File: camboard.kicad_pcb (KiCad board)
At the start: 2 copper layers, 64 x 120.5 mm, 68 parts, among them J1 Conn_02x05_Odd_Even, J2 Conn_02x25_Counter_Clockwise, J3 Conn_02x12_Counter_Clockwise, J4 USB_B_Micro, J5 Conn_01x03, SW1 SW_Push, SW3 SW_SPST, U1 MK82FN256VLL15, U2 Serial-Flash, U3 TPS61169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

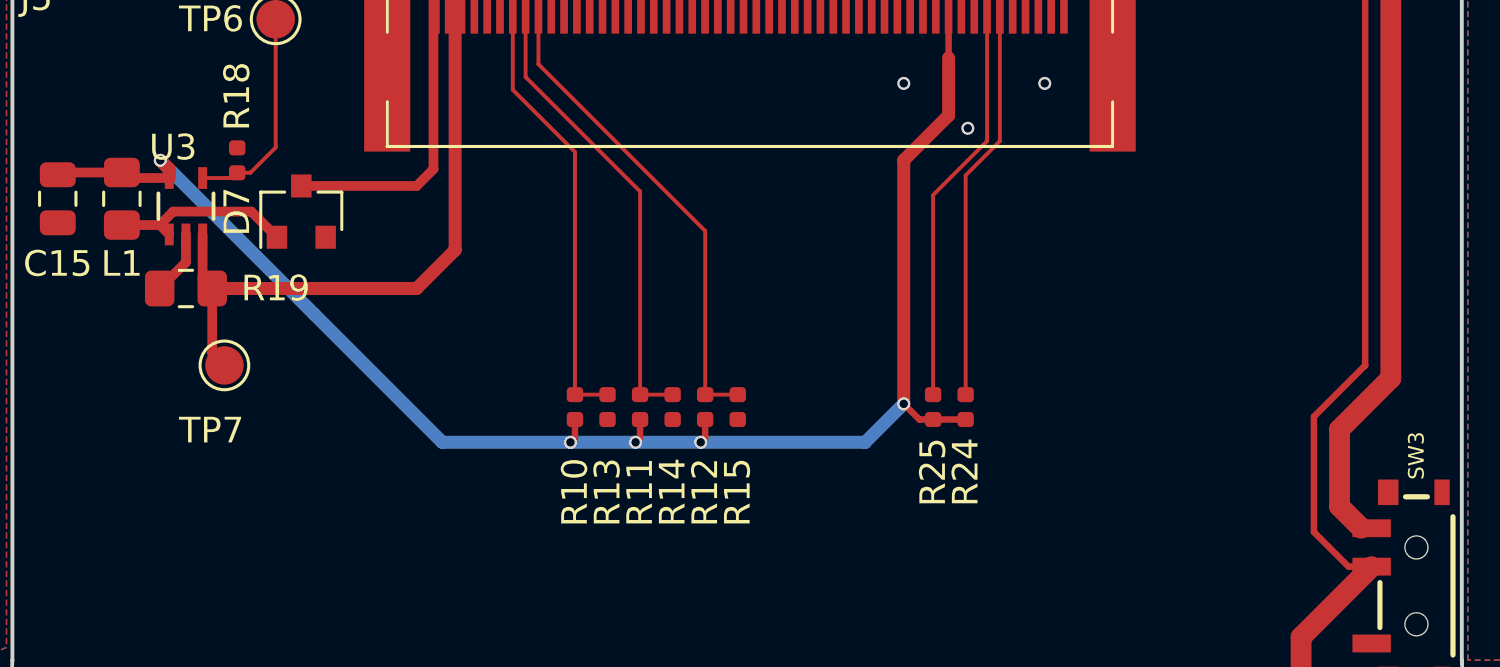
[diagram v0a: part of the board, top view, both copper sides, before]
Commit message: Power LCD backlight from VREG_IN, instead of 3.3 rail
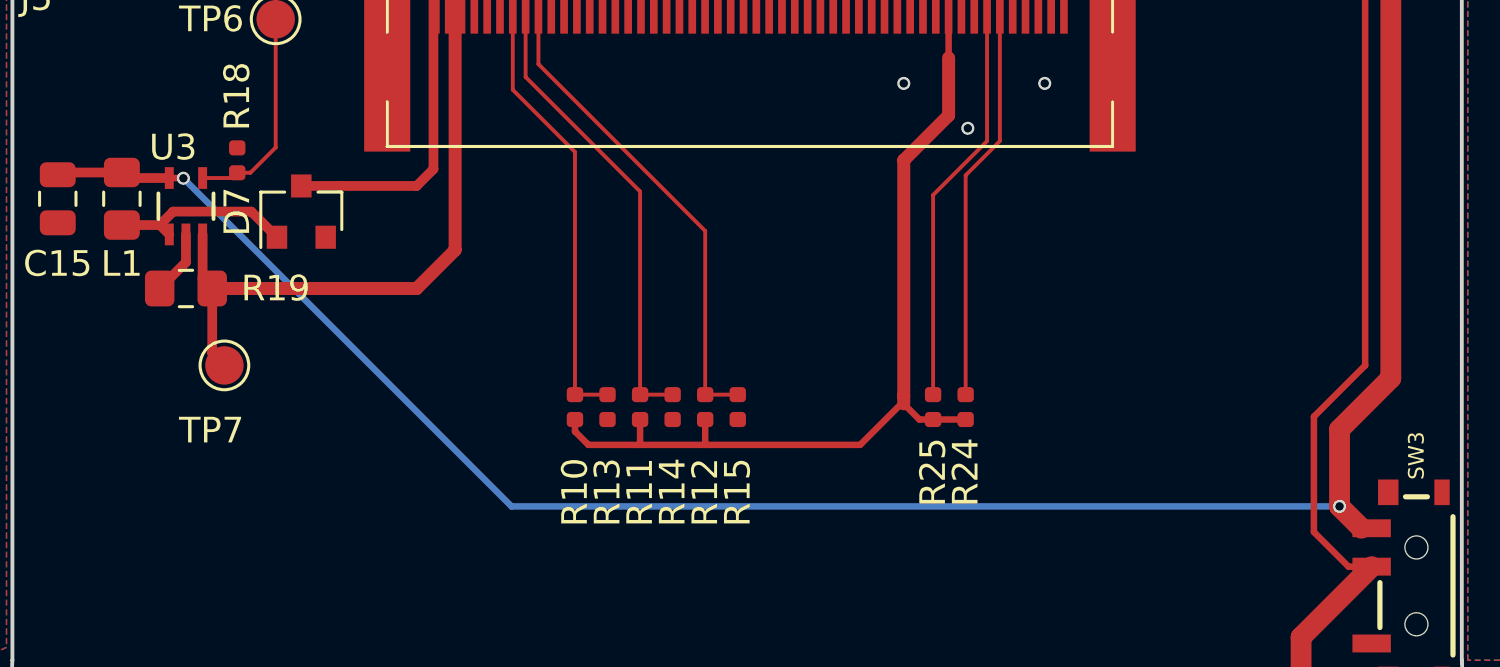
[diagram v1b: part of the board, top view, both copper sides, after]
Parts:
- R20: value 180 -> 91
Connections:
- C15 pad 1: +3V3 -> /VDD_REGIN
- L1 pad 1: +3V3 -> /VDD_REGIN
- U3 pad 5: +3V3 -> /VDD_REGIN
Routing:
- net /VDD_REGIN: track 119.2 -> 174.6 mm, vias 2 -> 4
- net +3V3: track 250.6 -> 224.6 mm, vias 19 -> 14
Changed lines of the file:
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@@
-(kicad_pcb (version 20171130) (host pcbnew 5.0.2-bee76a0~70~ubuntu18.10.1)
+(kicad_pcb (version 20171130) (host pcbnew 5.1.0-060a0da~80~ubuntu18.10.1)
   (general
     (thickness 1.6)
     (drawings 23)
-    (tracks 1000)
+    (tracks 999)
     (zones 0)
     (modules 68)
@@
     (zone_45_only no)
     (trace_min 0.1524)
-    (segment_width 0.2)
-    (edge_width 0.15)
     (via_size 0.508)
     (via_drill 0.3302)
@@
     (uvia_min_size 0.508)
     (uvia_min_drill 0.254)
+    (edge_width 0.15)
+    (segment_width 0.2)
     (pcb_text_width 0.3)
     (pcb_text_size 1.5 1.5)
@@
     )
     (pad 1 smd roundrect (at -0.9375 0 270) (size 0.975 1.4) (layers F.Cu F.Paste F.Mask) (roundrect_rratio 0.25)
-      (net 3 +3V3))
+      (net 10 /VDD_REGIN))
     (pad 2 smd roundrect (at 0.9375 0 270) (size 0.975 1.4) (layers F.Cu F.Paste F.Mask) (roundrect_rratio 0.25)
       (net 2 GND))
@@
     )
     (pad 1 smd roundrect (at -1.025 0 270) (size 1.15 1.4) (layers F.Cu F.Paste F.Mask) (roundrect_rratio 0.217391)
-      (net 3 +3V3))
+      (net 10 /VDD_REGIN))
     (pad 2 smd roundrect (at 1.025 0 270) (size 1.15 1.4) (layers F.Cu F.Paste F.Mask) (roundrect_rratio 0.217391)
       (net 87 "Net-(D7-Pad2)"))
@@
       (effects (font (size 1 1) (thickness 0.15)))
     )
-    (fp_text value 180 (at 0 1.17) (layer F.Fab) hide
+    (fp_text value 91 (at 0 1.17) (layer F.Fab) hide
       (effects (font (size 1 1) (thickness 0.15)))
     )
@@
       (net 73 /BKLT_PWM))
     (pad 5 smd rect (at 0 -2.2) (size 0.35 0.85) (layers F.Cu F.Paste F.Mask)
-      (net 3 +3V3))
+      (net 10 /VDD_REGIN))
   )
   (gr_text "cam-board v0.1" (at -18.2 -40.6) (layer F.SilkS)
@@
   (via (at -5 8.75) (size 0.508) (drill 0.3302) (layers F.Cu B.Cu) (net 2))
   (via (at 9 19.25) (size 0.508) (drill 0.3302) (layers F.Cu B.Cu) (net 2))
-  (segment (start -1.245142 31.325142) (end -1.42 31.5) (width 0.254) (layer F.Cu) (net 3))
-  (via (at -1.42 31.5) (size 0.508) (drill 0.3302) (layers F.Cu B.Cu) (net 3))
-  (segment (start -1.245142 30.610623) (end -1.245142 31.325142) (width 0.254) (layer F.Cu) (net 3))
-  (segment (start -3.785142 31.325142) (end -3.96 31.5) (width 0.254) (layer F.Cu) (net 3))
-  (via (at -3.96 31.5) (size 0.508) (drill 0.3302) (layers F.Cu B.Cu) (net 3))
-  (segment (start -3.785142 30.610623) (end -3.785142 31.325142) (width 0.254) (layer F.Cu) (net 3))
   (segment (start 9.409058 -11.439376) (end 9.560624 -11.439376) (width 0.254) (layer F.Cu) (net 3))
   (segment (start 9.366257 -11.482177) (end 9.409058 -11.439376) (width 0.254) (layer F.Cu) (net 3))
@@
   (segment (start 2.515 -15.902572) (end 2.515 -16) (width 0.254) (layer F.Cu) (net 3))
   (segment (start 3.118582 -15.29899) (end 2.515 -15.902572) (width 0.254) (layer F.Cu) (net 3))
-  (segment (start -23.784377 21.190623) (end -24 20.975) (width 0.381) (layer F.Cu) (net 3))
-  (segment (start -22.150142 21.190623) (end -23.784377 21.190623) (width 0.381) (layer F.Cu) (net 3))
-  (segment (start -26.4125 20.975) (end -26.5 21.0625) (width 0.381) (layer F.Cu) (net 3))
-  (segment (start -24 20.975) (end -26.4125 20.975) (width 0.381) (layer F.Cu) (net 3))
+  (segment (start -23.784377 21.190623) (end -24 20.975) (width 0.381) (layer F.Cu) (net 10))
+  (segment (start -22.150142 21.190623) (end -23.784377 21.190623) (width 0.381) (layer F.Cu) (net 10))
+  (segment (start -26.4125 20.975) (end -26.5 21.0625) (width 0.381) (layer F.Cu) (net 10))
+  (segment (start -24 20.975) (end -26.4125 20.975) (width 0.381) (layer F.Cu) (net 10))
   (segment (start 8.75 13.61) (end 7.75 13.61) (width 0.1524) (layer F.Cu) (net 3))
   (segment (start 8.25 16.5) (end 8.25 16.75) (width 0.254) (layer F.Cu) (net 3))
@@
   (segment (start 7.110623 30.610623) (end 8.914858 30.610623) (width 0.254) (layer F.Cu) (net 3))
   (segment (start 6.5 30) (end 7.110623 30.610623) (width 0.254) (layer F.Cu) (net 3))
-  (via (at -6.5 31.5) (size 0.508) (drill 0.3302) (layers F.Cu B.Cu) (net 3))
-  (segment (start -6.325142 30.610623) (end -6.325142 31.325142) (width 0.254) (layer F.Cu) (net 3))
-  (segment (start -6.325142 31.325142) (end -6.5 31.5) (width 0.254) (layer F.Cu) (net 3))
-  (segment (start -6.5 31.5) (end -1.42 31.5) (width 0.508) (layer B.Cu) (net 3))
-  (segment (start -1.42 31.5) (end 5 31.5) (width 0.508) (layer B.Cu) (net 3))
-  (via (at 6.5 30) (size 0.508) (drill 0.3302) (layers F.Cu B.Cu) (net 3))
-  (segment (start 5 31.5) (end 6.5 30) (width 0.508) (layer B.Cu) (net 3))
-  (via (at -22.5 20.5) (size 0.508) (drill 0.3302) (layers F.Cu B.Cu) (net 3))
-  (segment (start -22.150142 20.849858) (end -22.5 20.5) (width 0.508) (layer F.Cu) (net 3))
-  (segment (start -22.150142 21.190623) (end -22.150142 20.849858) (width 0.508) (layer F.Cu) (net 3))
   (via (at 0 -12.5) (size 0.508) (drill 0.3302) (layers F.Cu B.Cu) (net 3))
   (via (at 8 11) (size 0.508) (drill 0.3302) (layers F.Cu B.Cu) (net 3))
@@
   (segment (start -11.515 -0.735) (end -11.515 -1) (width 0.254) (layer F.Cu) (net 3))
   (segment (start -12.485 0.235) (end -11.515 -0.735) (width 0.254) (layer F.Cu) (net 3))
-  (segment (start -11.5 31.5) (end -6.5 31.5) (width 0.508) (layer B.Cu) (net 3))
-  (segment (start -22.5 20.5) (end -16.5 26.5) (width 0.508) (layer B.Cu) (net 3))
-  (segment (start -16.5 26.5) (end -11.5 31.5) (width 0.508) (layer B.Cu) (net 3))
   (segment (start 8.25 18.75) (end 8.25 16.5) (width 0.508) (layer F.Cu) (net 3))
-  (segment (start 6.5 30) (end 6.5 20.5) (width 0.508) (layer F.Cu) (net 3))
   (segment (start 6.5 20.5) (end 8.25 18.75) (width 0.508) (layer F.Cu) (net 3))
+  (segment (start 6.5 29.7) (end 6.5 20.5) (width 0.508) (layer F.Cu) (net 3))
+  (segment (start 6.5 30) (end 6.5 29.7) (width 0.508) (layer F.Cu) (net 3))
+  (segment (start -5.8 31.6) (end -6.325142 31.074858) (width 0.254) (layer F.Cu) (net 3))
+  (segment (start -6.325142 31.074858) (end -6.325142 30.610623) (width 0.254) (layer F.Cu) (net 3))
+  (segment (start 6.5 29.7) (end 6.5 29.9) (width 0.254) (layer F.Cu) (net 3))
+  (segment (start 6.5 29.9) (end 4.8 31.6) (width 0.254) (layer F.Cu) (net 3))
+  (segment (start -3.785142 31.585142) (end -3.8 31.6) (width 0.254) (layer F.Cu) (net 3))
+  (segment (start -3.785142 30.610623) (end -3.785142 31.585142) (width 0.254) (layer F.Cu) (net 3))
+  (segment (start -3.8 31.6) (end -5.8 31.6) (width 0.254) (layer F.Cu) (net 3))
+  (segment (start -1.245142 31.554858) (end -1.2 31.6) (width 0.254) (layer F.Cu) (net 3))
+  (segment (start -1.245142 30.610623) (end -1.245142 31.554858) (width 0.254) (layer F.Cu) (net 3))
+  (segment (start 4.8 31.6) (end -1.2 31.6) (width 0.254) (layer F.Cu) (net 3))
+  (segment (start -1.2 31.6) (end -3.8 31.6) (width 0.254) (layer F.Cu) (net 3))
   (via (at -14 71) (size 1.905) (drill 0.4) (layers F.Cu B.Cu) (net 4))
   (via (at -16 71) (size 1.905) (drill 0.4) (layers F.Cu B.Cu) (net 4))
@@
   (segment (start -0.890143 -14.890143) (end -1 -15) (width 0.254) (layer F.Cu) (net 10))
   (segment (start -0.890143 -13.686377) (end -0.890143 -14.890143) (width 0.254) (layer F.Cu) (net 10))
+  (via (at 23.5 34) (size 0.508) (drill 0.3302) (layers F.Cu B.Cu) (net 10))
+  (via (at -21.6 21.2) (size 0.508) (drill 0.3302) (layers F.Cu B.Cu) (net 10))
+  (segment (start -22.150142 21.190623) (end -21.609377 21.190623) (width 0.254) (layer F.Cu) (net 10))
+  (segment (start -21.609377 21.190623) (end -21.6 21.2) (width 0.254) (layer F.Cu) (net 10))
+  (segment (start -8.8 34) (end 23.5 34) (width 0.254) (layer B.Cu) (net 10))
+  (segment (start -21.6 21.2) (end -8.8 34) (width 0.254) (layer B.Cu) (net 10))
   (segment (start -21 0.390765) (end -23.520142 -2.129377) (width 0.254) (layer F.Cu) (net 11) (status 30))
   (segment (start -21 0.4) (end -21 0.390765) (width 0.254) (layer F.Cu) (net 11) (status 30))
